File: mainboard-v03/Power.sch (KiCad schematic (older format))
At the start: 36 parts, among them Q1 IRLML2803, U4 MAX4372TEUK+T, U5 TPS54226PWPRPWP14_2P31X2P46-L, U6 LTC4121, U7 NDS8434

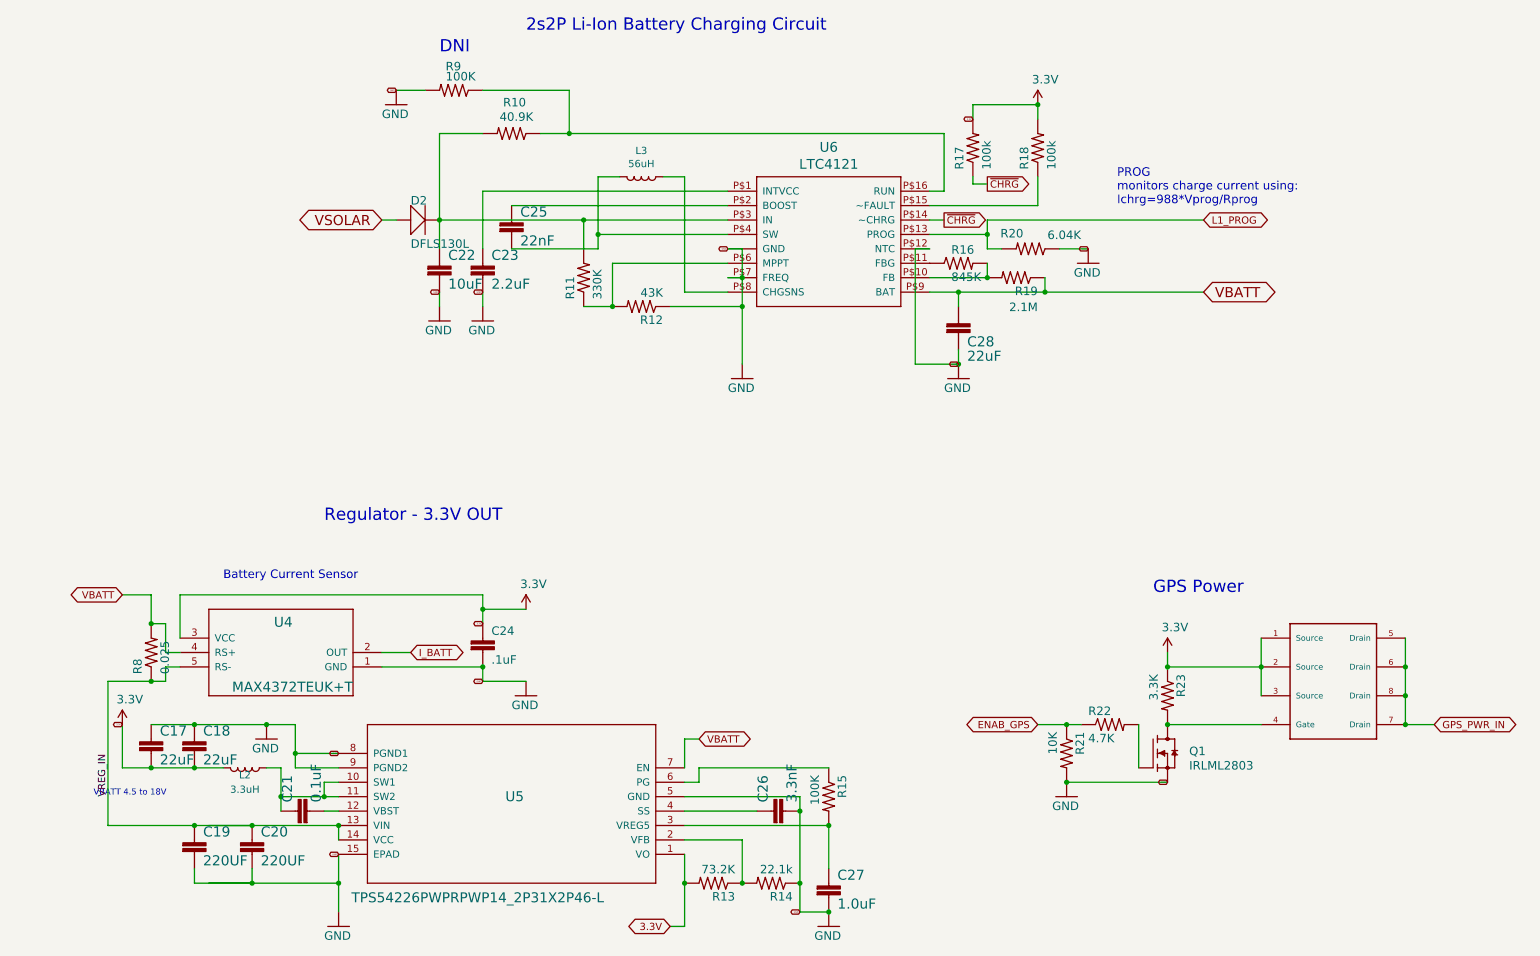
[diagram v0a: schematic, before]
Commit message: cleaning up schematic scheets
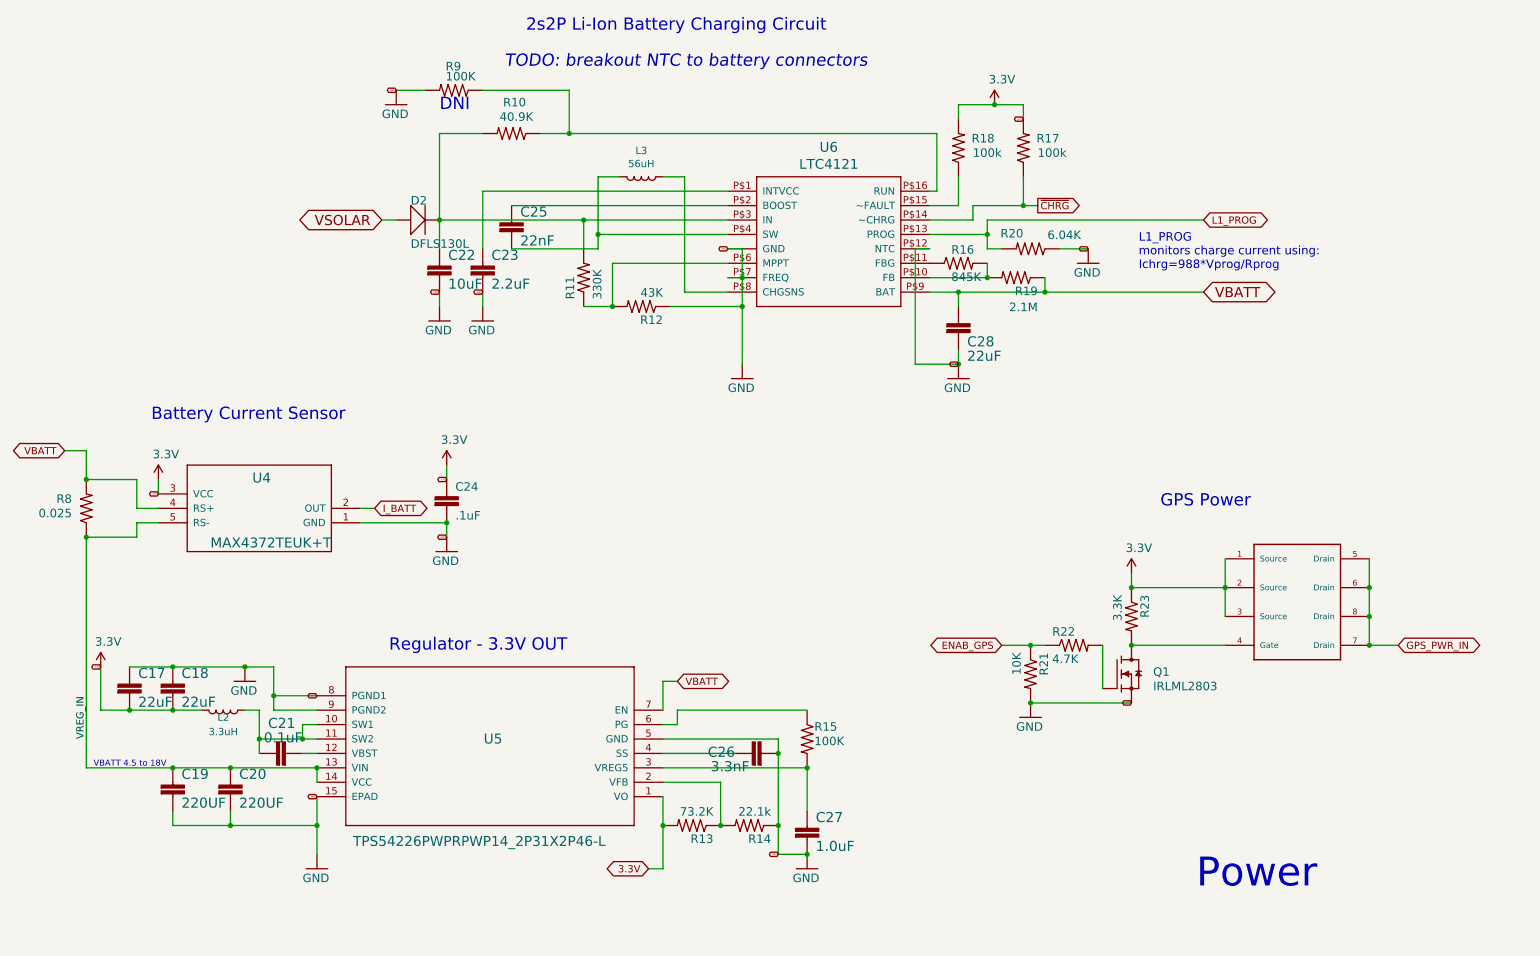
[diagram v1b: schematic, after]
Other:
- note added: "L1_PROG\nmonitors charge current using:\nIchrg=988*Vprog/Rprog\n"
- note added: "Power"
- note added: "TODO: breakout NTC to battery connectors"
- note removed: "PROG\nmonitors charge current using:\nIchrg=988*Vprog/Rprog\n"
- moved on the sheet: C17, C18, C19, C20, C21, C24, C26, C27, L2, Q1, R13, R14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
